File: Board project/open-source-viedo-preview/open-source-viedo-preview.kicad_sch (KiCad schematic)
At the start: 0 parts

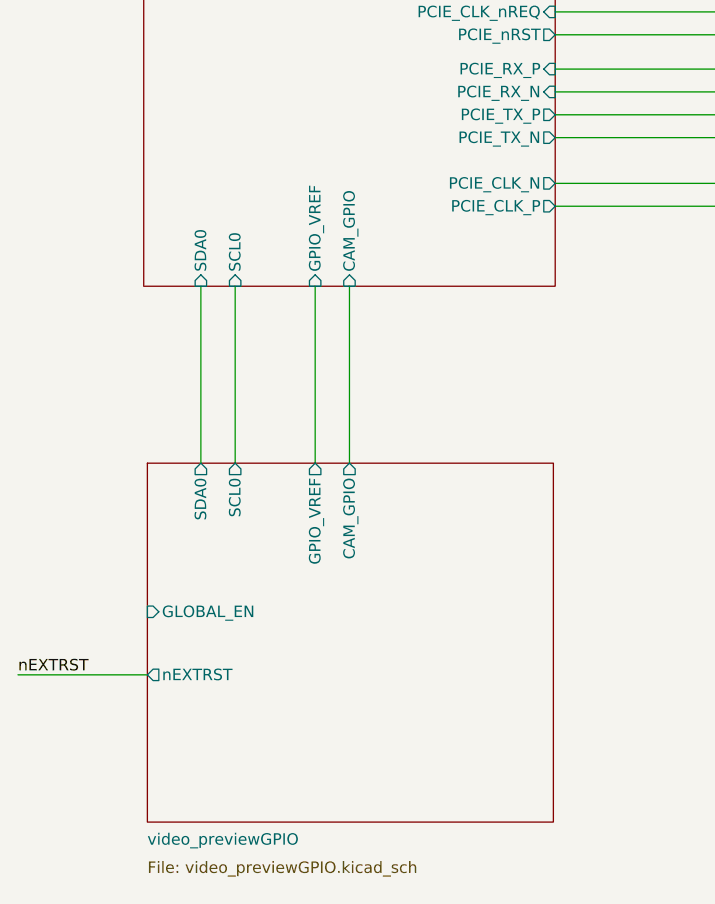
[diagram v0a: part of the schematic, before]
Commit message: ERC error repaired
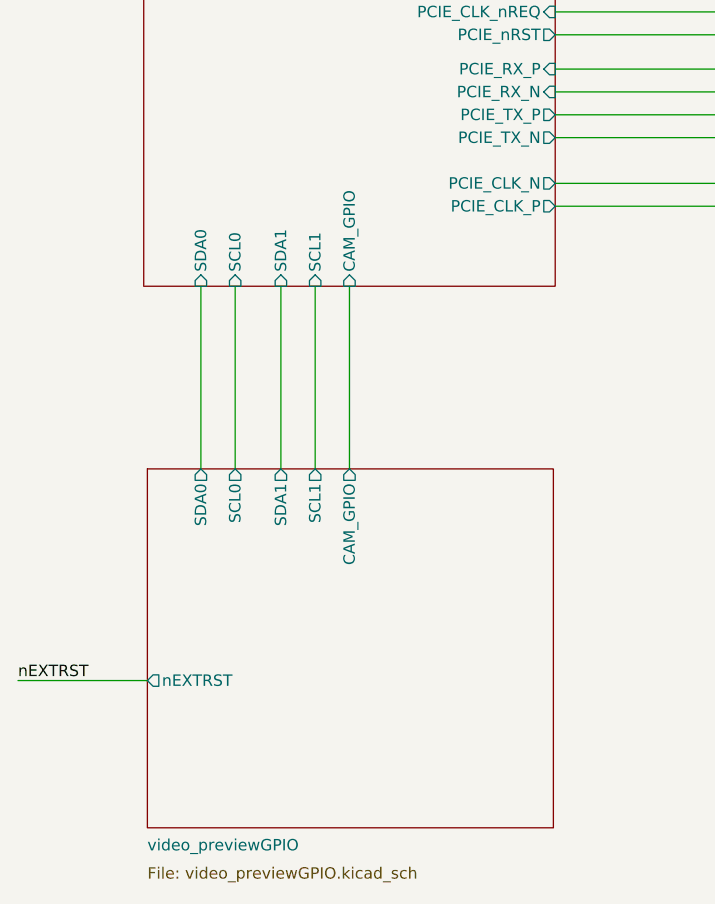
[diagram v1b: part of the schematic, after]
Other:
- sheet video_previewGPIO ports: added SCL1, SDA1; removed GLOBAL_EN, GPIO_VREF
- sheet video_preview_HighSpeed ports: added SCL1, SDA1; removed GPIO_VREF
